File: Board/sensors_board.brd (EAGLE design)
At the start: 34 x 30 mm, 7 parts, among them U1 TEM-HUM-AM2302(4P-25.0X15.0MM)

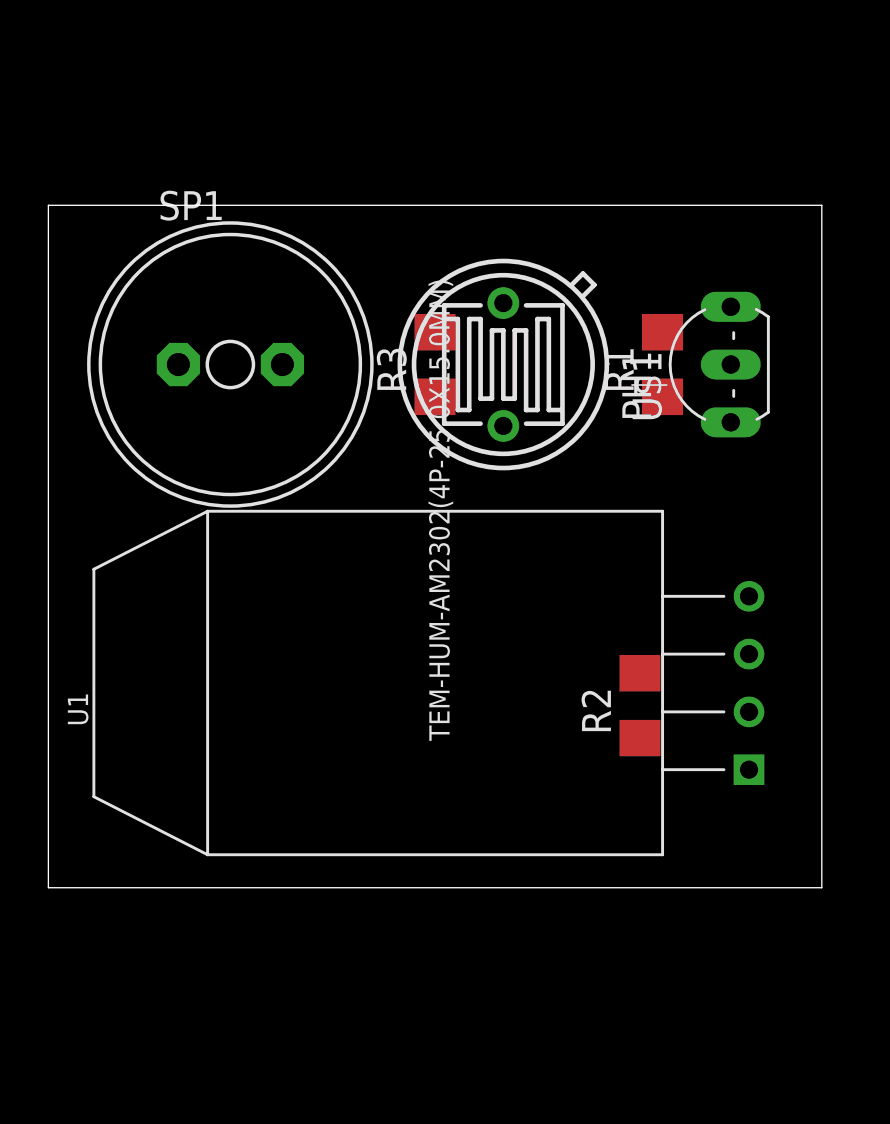
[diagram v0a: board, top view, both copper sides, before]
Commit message: Add new files
- motherboard scheme
- ATtiny13 code
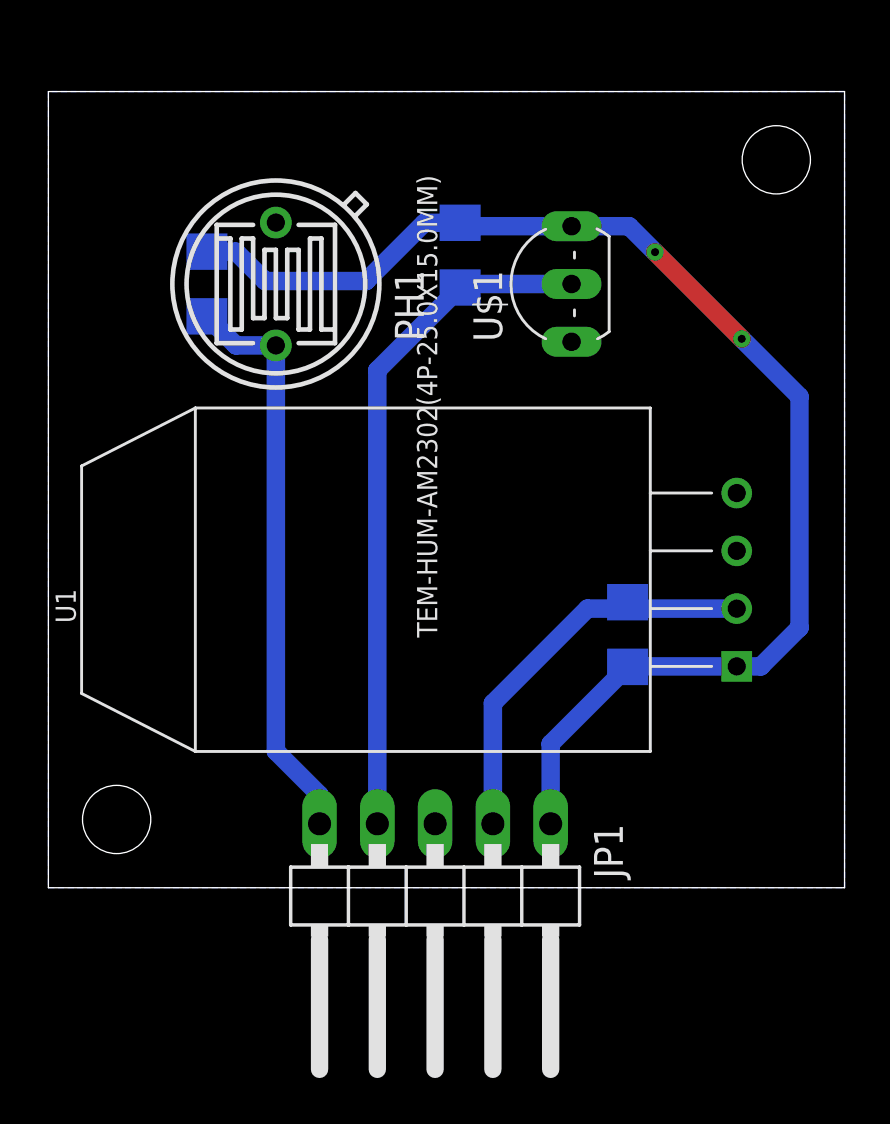
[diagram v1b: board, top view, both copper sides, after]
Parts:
- removed SP1: AL11P, buzzer:AL11P
- added JP1: (no value), pinhead:1X05/90
- moved R3 10.6 mm to (6.97, 26.5), flipped to the bottom
- moved PH1 10.6 mm to (10.0, 26.5)
- moved R1 10.1 mm to (18.1, 27.8), flipped to the bottom
- moved U$1 7.84 mm to (23.0, 26.5)
- moved U1 4.57 mm to (16.5, 13.5)
- moved R2 3.18 mm to (25.5, 11.1), flipped to the bottom, turned to 270 degrees
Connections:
- removed net VDD: U$1.1
- new net +3V3: JP1.1, R1.2, R2.2, R3.2, U$1.1, U1.P$1
- new net N$1: JP1.2, R2.1, U1.P$2
- new net N$2: JP1.4, R1.1, U$1.2
- new net N$3: JP1.5, PH1.1, R3.1
- net GND: now also JP1.3, PH1.2, U1.P$4
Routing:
- net +3V3: track 0.00 -> 57.6 mm, vias 0 -> 2
- net N$2: track 0.00 -> 30.0 mm
- net N$3: track 0.00 -> 25.4 mm
- net N$1: track 0.00 -> 18.1 mm
- added copper zone on layer 16, net GND
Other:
- board size 34 x 30 mm -> 35 x 35 mm
